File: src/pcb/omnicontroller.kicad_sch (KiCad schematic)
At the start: 47 parts, among them J1 G-Switch GT-USB-7010ASV, U1 RP2040, U2 NCP1117ST33T3G, U3 W25Q128JVSIM, X1 SW_Omron_B3FS-1000P, Y1 ABM8-272-T3, Y2 SW_Omron_B3FS-1000P

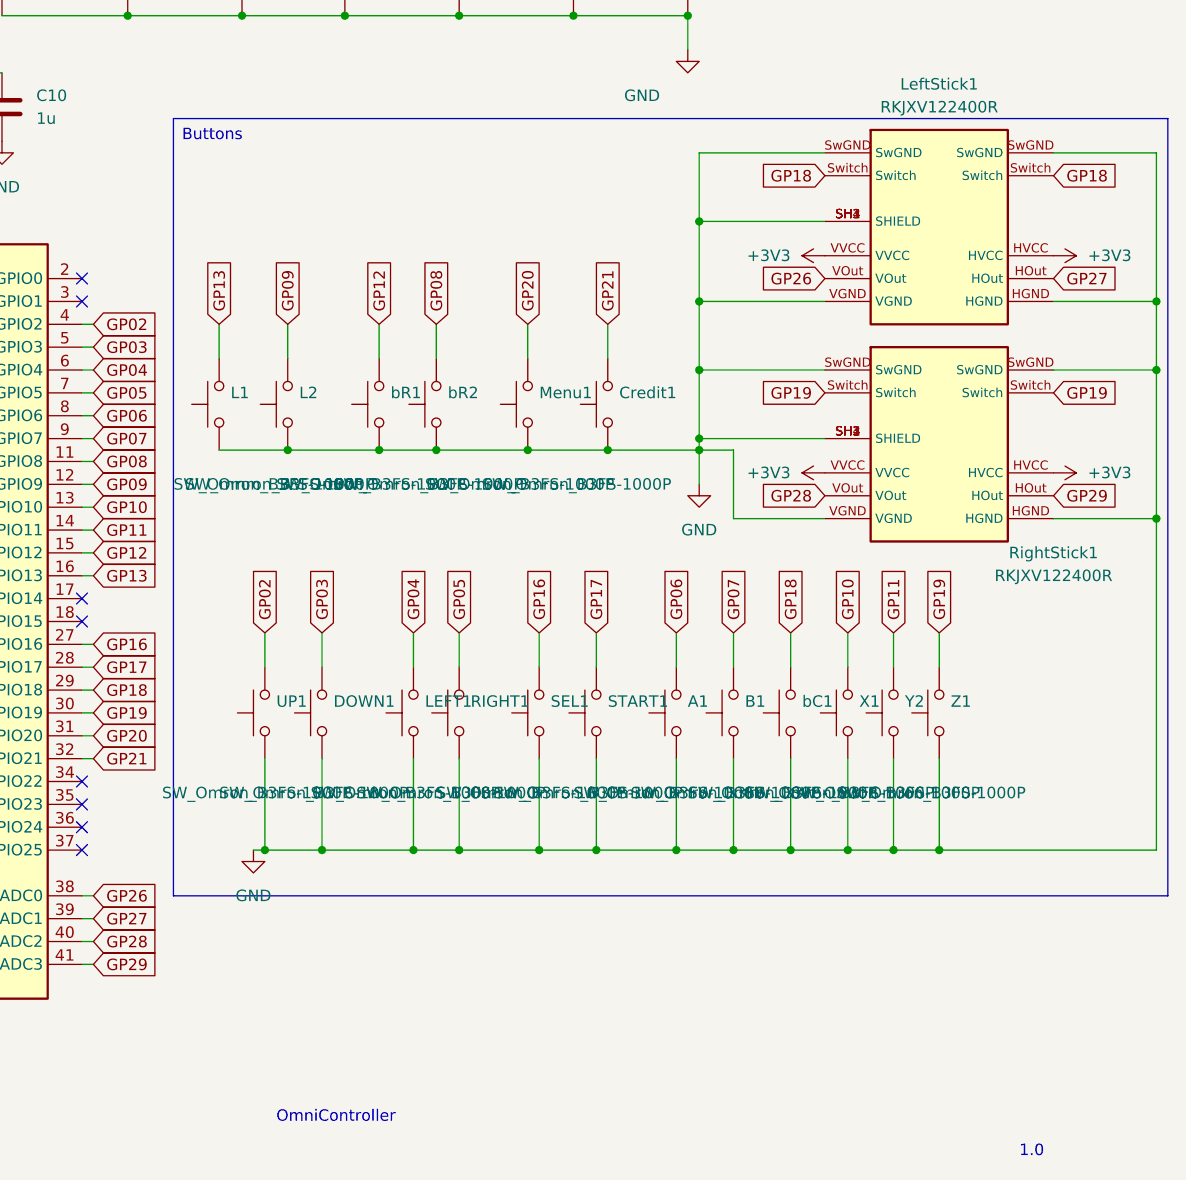
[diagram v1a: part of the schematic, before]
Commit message: move L1,L2, R1 and R2 buttons to top side
replace B3FS-1000 with B3F-3100 for those buttons
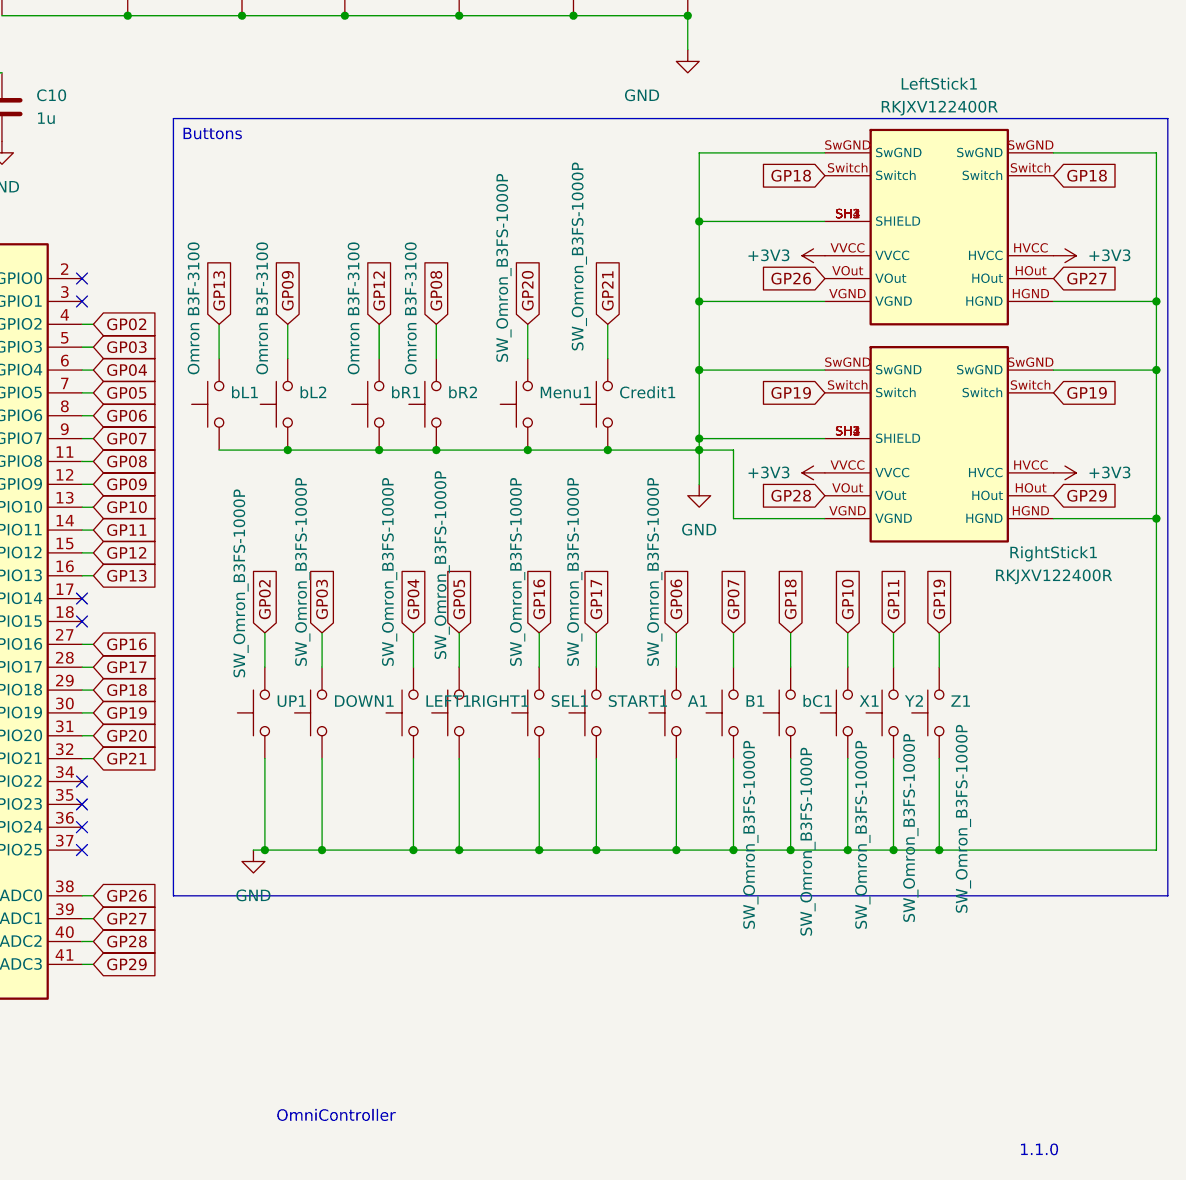
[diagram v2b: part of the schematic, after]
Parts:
- removed L1, L2: SW_Omron_B3FS-1000P, Button_Switch_SMD:SW_SPST_Omron_B3FS-100xP, symbol Switch:SW_Omron_B3FS
- added bL1, bL2: SW_B3F-3100, Buttons:SW_B3F-3100, symbol Switch:SW_Omron_B3FS
- bR1, bR2: value SW_Omron_B3FS-1000P -> SW_B3F-3100; footprint Button_Switch_SMD:SW_SPST_Omron_B3FS-100xP -> Buttons:SW_B3F-3100
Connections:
- net GND: now also bL1.1, bL2.1
- net GP09: now also bL2.2
- net GP13: now also bL1.2
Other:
- note added: "1.1.0"
- note removed: "1.0"

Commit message: connect buttons C and Z to GPIO 22 and 23
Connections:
- net GP18: no longer bC1.2
- net GP19: no longer Z1.2
- net GP22: now reaches U1.34 (GPIO22)
- net GP22: now also bC1.2
- net GP23: now reaches U1.35 (GPIO23)
- net GP23: now also Z1.2
- no-connect marks 14 -> 12
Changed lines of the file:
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@@
 	)
 	(no_connect
-		(at 165.1 152.4)
-	)
-	(no_connect
 		(at 114.3 162.56)
 	)
@@
 	)
 	(no_connect
-		(at 165.1 154.94)
-	)
-	(no_connect
 		(at 165.1 157.48)
 	)
@@
 	(wire
 		(pts
+			(xy 165.1 152.4) (xy 166.37 152.4)
+		)
+		(stroke
+			(width 0)
+			(type default)
+		)
+	)
+	(wire
+		(pts
 			(xy 219.71 59.69) (xy 232.41 59.69)
 		)
@@
 	(wire
 		(pts
+			(xy 165.1 154.94) (xy 166.37 154.94)
+		)
+		(stroke
+			(width 0)
+			(type default)
+		)
+	)
+	(wire
+		(pts
 			(xy 245.11 41.91) (xy 252.73 41.91)
 		)
@@
 		)
 	)
+	(global_label "GP22"
+		(shape input)
+		(at 166.37 152.4 0)
+		(fields_autoplaced yes)
+		(effects
+			(font
+				(size 1.27 1.27)
+			)
+			(justify left)
+		)
+		(property "Intersheetrefs" "${INTERSHEET_REFS}"
+			(at 174.3142 152.4 0)
+			(effects
+				(font
+					(size 1.27 1.27)
+				)
+				(justify left)
+				(hide yes)
+			)
+		)
+	)
 	(global_label "USB_DM"
 		(shape input)
@@
 		)
 	)
-	(global_label "GP18"
+	(global_label "GP22"
 		(shape input)
 		(at 243.84 135.89 90)
@@
 		)
 	)
+	(global_label "GP23"
+		(shape input)
+		(at 166.37 154.94 0)
+		(fields_autoplaced yes)
+		(effects
+			(font
+				(size 1.27 1.27)
+			)
+			(justify left)
+		)
+		(property "Intersheetrefs" "${INTERSHEET_REFS}"
+			(at 174.3142 154.94 0)
+			(effects
+				(font
+					(size 1.27 1.27)
+				)
+				(justify left)
+				(hide yes)
+			)
+		)
+	)
 	(global_label "GP08"
 		(shape input)
@@
 		)
 	)
-	(global_label "GP19"
+	(global_label "GP23"
 		(shape input)
 		(at 260.35 135.89 90)

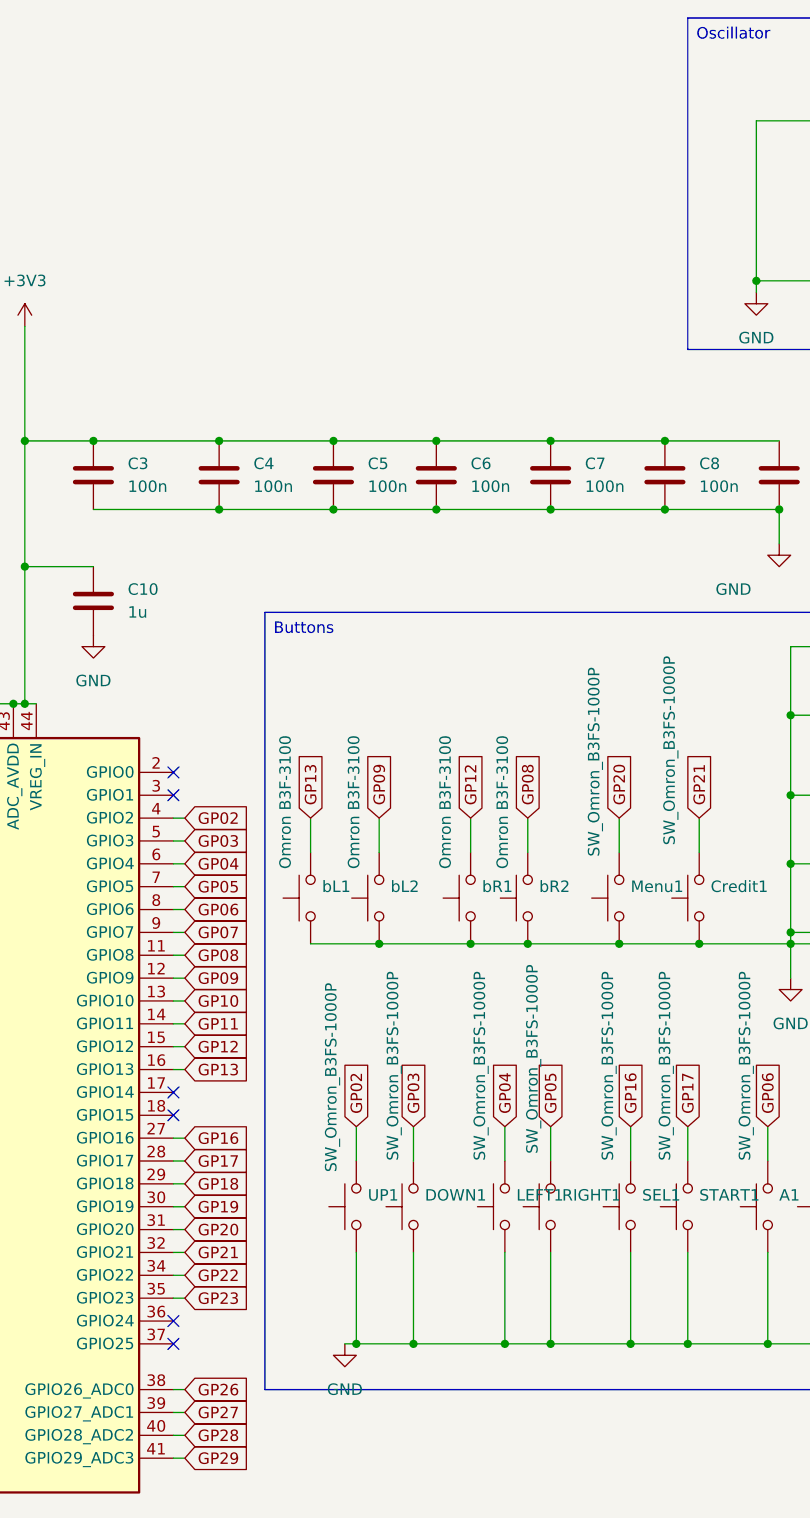
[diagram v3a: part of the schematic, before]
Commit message: add USB A port for PS4/5 host mode authentication
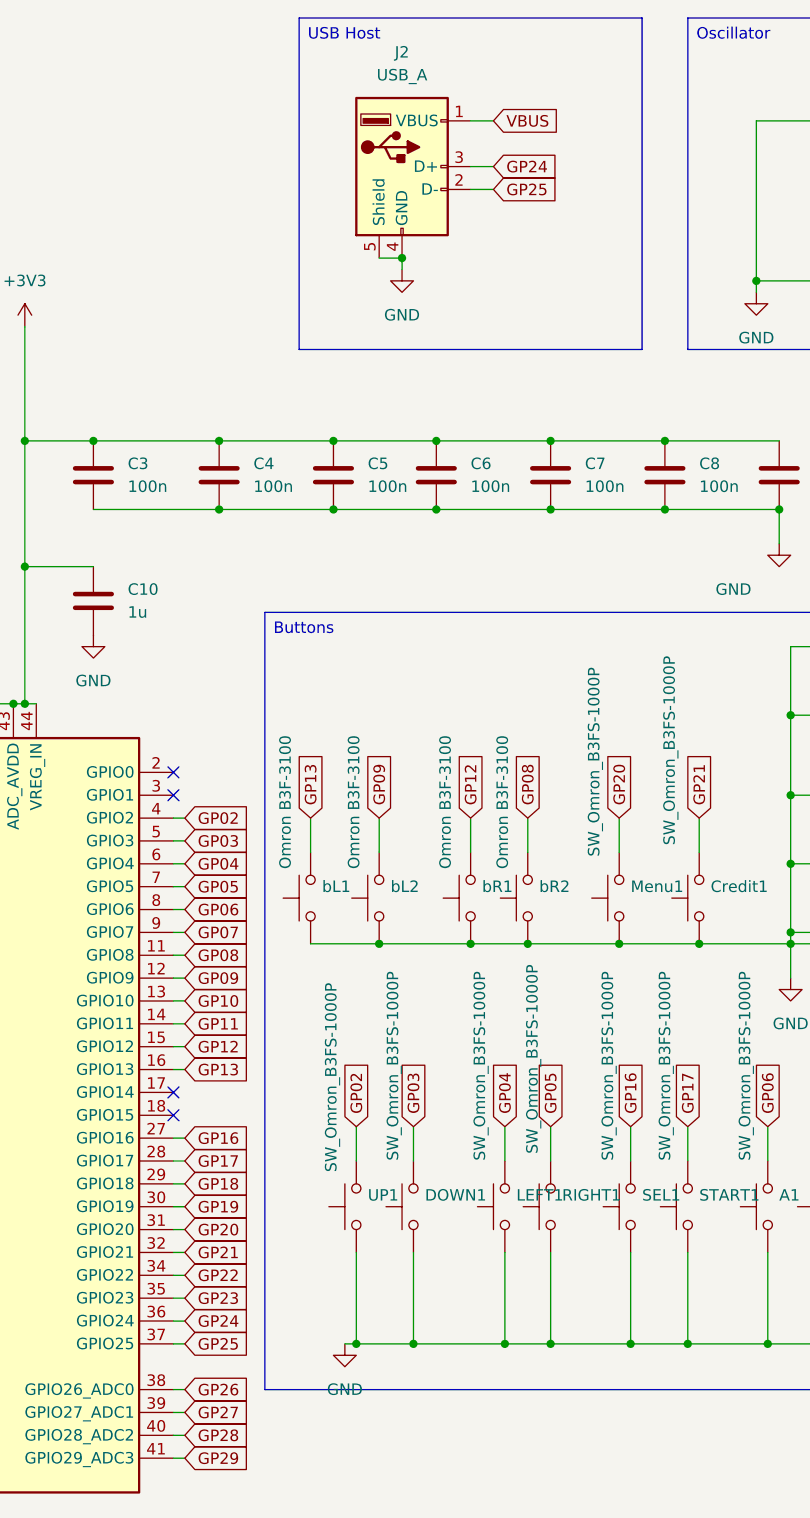
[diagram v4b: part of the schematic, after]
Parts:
- added J2: USB_A, Connector_USB:USB_A_Receptacle_GCT_USB1046, symbol Connector:USB_A
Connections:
- net GND: now also J2.4 (GND), J2.5 (Shield)
- net VBUS: now also J2.1 (VBUS)
- net GP24: now reaches U1.36 (GPIO24)
- net GP24: now also J2.3 (D+)
- net GP25: now reaches U1.37 (GPIO25)
- net GP25: now also J2.2 (D-)
- no-connect marks 12 -> 10

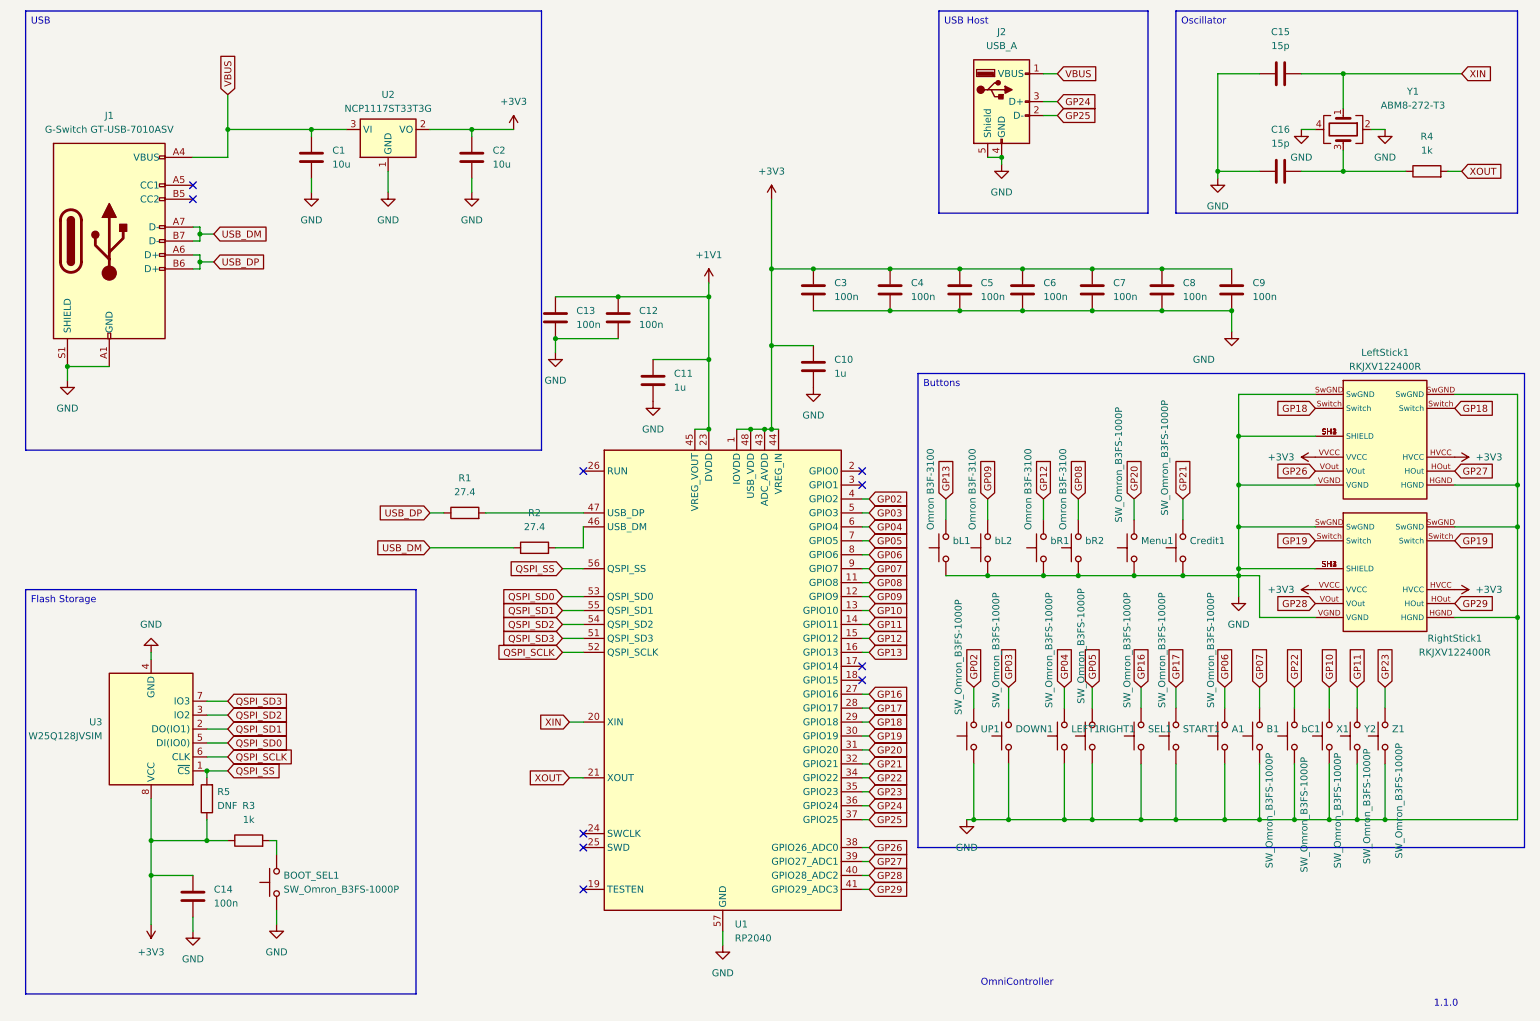
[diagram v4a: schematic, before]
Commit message: add pinheader with all unused GPIO
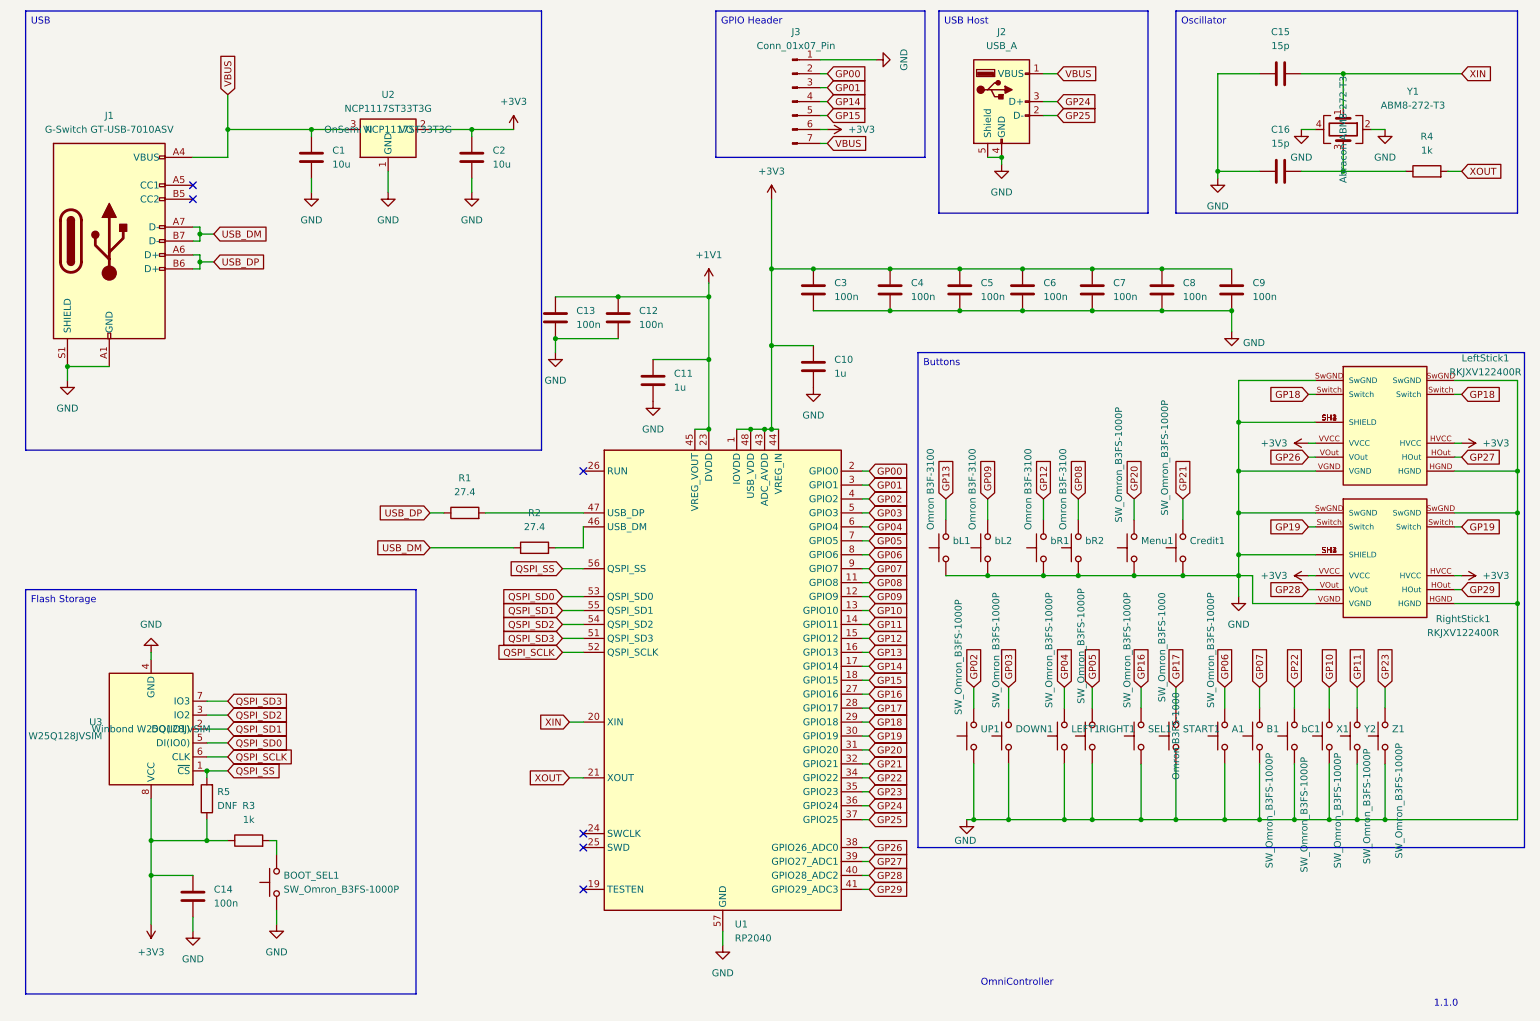
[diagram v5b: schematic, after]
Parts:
- added J3: Conn_01x07_Pin, Connector_PinHeader_2.54mm:PinHeader_1x07_P2.54mm_Horizontal, symbol Connector:Conn_01x07_Pin
- LeftStick1, RightStick1: symbol Controllers_library:ALPS_Electric_RKJXV1220001 -> SW_RKJXV122400R:RKJXV122400R; Availability (none) -> In Stock; Check_prices (none) -> https://www.snapeda.com/parts/RKJXV122400R/ALPS/view-part/?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; Description_1 (none) -> Multi-Directional Switches 23degree max, 10Kohm 50V AC, 5V 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; MANUFACTURER (none) -> ALPS; MAXIMUM_PACKAGE_HEIGHT (none) -> 19.8 mm; MF (none) -> Alps Alpine; MP (none) -> RKJXV122400R; PARTREV (none) -> N/A; Package (none) -> None; Price (none) -> None; SNAPEDA_PN (none) -> RKJXV122400R; STANDARD (none) -> Manufacturer Recommendations; SnapEDA_Link (none) -> https://www.snapeda.com/parts/RKJXV122400R/ALPS/view-part/?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
- START1: value SW_Omron_B3FS-1000P -> SW_Omron_B3FS-1000
- U3: footprint Package_SO:SOIC-8_5.23x5.23mm_P1.27mm -> Package_SO:SOIC-8_5.3x5.3mm_P1.27mm
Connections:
- net +3V3: now also J3.6 (Pin_6)
- net GND: now also J3.1 (Pin_1)
- net VBUS: now also J3.7 (Pin_7)
- net GP14: now reaches U1.17 (GPIO14)
- net GP14: now also J3.4 (Pin_4)
- net GP15: now reaches U1.18 (GPIO15)
- net GP15: now also J3.5 (Pin_5)
- net GP00: now reaches U1.2 (GPIO0)
- net GP00: now also J3.2 (Pin_2)
- net GP01: now reaches U1.3 (GPIO1)
- net GP01: now also J3.3 (Pin_3)
- no-connect marks 10 -> 6
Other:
- moved on the sheet: LeftStick1, RightStick1
